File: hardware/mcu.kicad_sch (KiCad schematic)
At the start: 28 parts, among them J2 DS1021-1X3SF11-B, SW1 BOOT / PTS810, SW2 RESET / PTS810, U2 ESP32-C6-WROOM-1, U4 RV-3028-C7

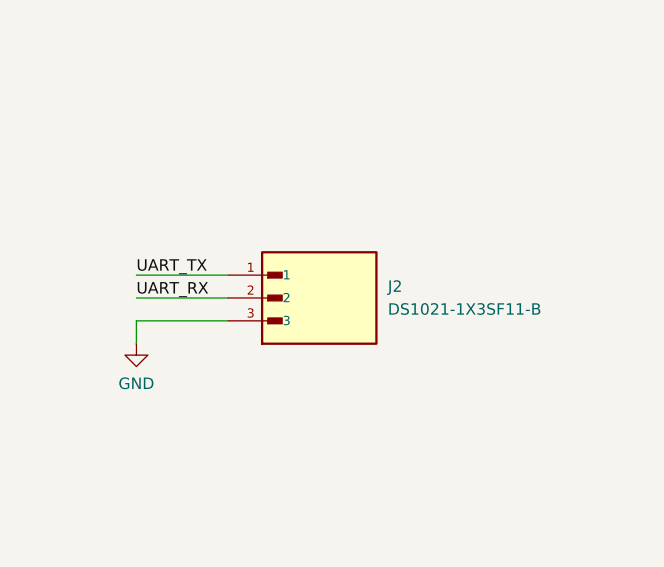
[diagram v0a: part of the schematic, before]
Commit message: J2 UART başlığını test noktalarıyla değiştir, ESP32 sembolünü yerelleştir
Kütüphane tabloları artık tamamen ${KIPRJMOD} göreli: harici mutlak yol
veya eksik kütüphane kalmadı, proje başka bir makinede olduğu gibi açılır.

J2 -> TP11/TP12/TP13
- J2 (DS1021-1X3SF11-B, 3 pinli UART başlığı) sembolü ve lib_symbols
  önbelleği mcu.kicad_sch'ten kaldırıldı.
- Yerine Connector:TestPoint ile TP11 (UART_TX), TP12 (UART_RX) ve
  TP13 (GND) eklendi; her biri J2'nin pinlerinin bulunduğu tellere bağlı.
- Sembol kütüphanesi başka bir makinenin Windows indirme klasörünü
  gösterdiği için sym-lib-table kaydı düştü; artık kullanılmayan
  CONNFLY_DS1021-1X3SF11-B footprint kütüphanesi de kaldırıldı.

ESP32-C6-WROOM-1 yerel kopya
- Sembol şematiğin lib_symbols önbelleğinden çıkarıldı, footprint
  espressif/kicad-libraries deposundan alındı; ikisi de
  hardware/libraries/PCM_Espressif.* altında.
- Takma ad şematiktekiyle aynı tutuldu, bu yüzden şematik düzenlemesi
  gerekmedi. Depoyu klonlayan birinin artık KiCad PCM eklentisini ayrıca
  kurması gerekmiyor.

Doğrulama
- Netlist karşılaştırması: 90 net sabit, yalnızca 3'ü değişti ve her biri
  birebir takas - J2.1->TP11.1, J2.2->TP12.1, J2.3->TP13.1.
- Sembolün 29 pini ile footprint'in 29 pad'i tam örtüşüyor.
- kicad-cli ERC: 7 -> 4 ihlal. Düşen üçü DS1021 ve iki PCM_Espressif
  uyarısı. Kalan 4 ihlal bu değişiklikten önce de vardı.

Co-Authored-By: Claude Opus 5 <noreply@anthropic.com>
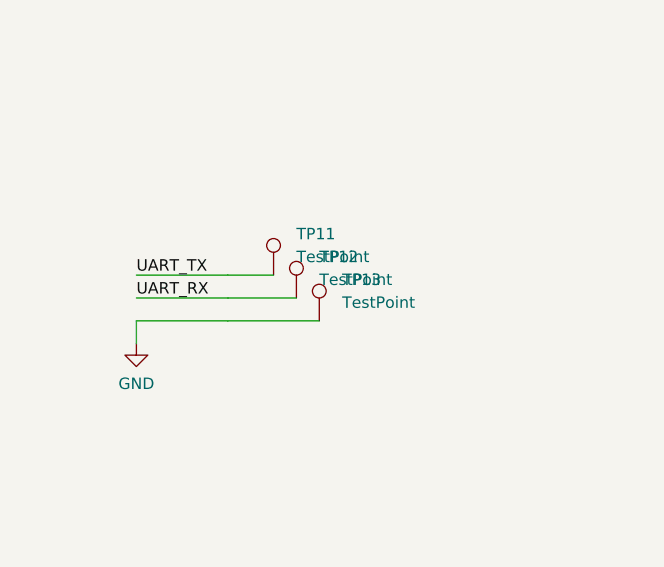
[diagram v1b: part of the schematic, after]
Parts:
- removed J2: DS1021-1X3SF11-B, CONNFLY_DS1021-1X3SF11-B:CONNFLY_DS1021-1X3SF11-B, symbol DS1021-1X3SF11-B:DS1021-1X3SF11-B
- added TP11, TP12, TP13: TestPoint, TestPoint:TestPoint_Pad_D1.0mm, symbol Connector:TestPoint
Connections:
- net GND: now also TP13.1
- net UART_RX: now also TP12.1
- net UART_TX: now also TP11.1
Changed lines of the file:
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@@
-	)
-	(symbol
-		(lib_id "DS1021-1X3SF11-B:DS1021-1X3SF11-B")
-		(at 247.65 146.05 0)
-		(unit 1)
-		(body_style 1)
-		(exclude_from_sim no)
-		(in_bom yes)
-		(on_board yes)
-		(in_pos_files yes)
-		(dnp no)
-		(fields_autoplaced yes)
-		(property "Reference" "J2"
-			(at 255.27 144.7799 0)
-			(show_name no)
-			(do_not_autoplace no)
-			(effects
-				(font
-					(size 1.27 1.27)
-				)
-				(justify left)
-			)
-		)
-		(property "Value" "DS1021-1X3SF11-B"
-			(at 255.27 147.3199 0)
-			(show_name no)
-			(do_not_autoplace no)
-			(effects
-				(font
-					(size 1.27 1.27)
-				)
-				(justify left)
-			)
-		)
-		(property "Footprint" "CONNFLY_DS1021-1X3SF11-B:CONNFLY_DS1021-1X3SF11-B"
-			(at 247.65 146.05 0)
-			(hide yes)
-			(show_name no)
-			(do_not_autoplace no)
-			(effects
-				(font
-					(size 1.27 1.27)
-				)
-				(justify bottom)
-			)
-		)
-		(property "Datasheet" ""
-			(at 247.65 146.05 0)
-			(hide yes)
-			(show_name no)
-			(do_not_autoplace no)
-			(effects
-				(font
-					(size 1.27 1.27)
-				)
-			)
-		)
-		(property "Description" "3 position 2.54mm single row vertical pin header through hole"
-			(at 247.65 146.05 0)
-			(hide yes)
-			(show_name no)
-			(do_not_autoplace no)
-			(effects
-				(font
-					(size 1.27 1.27)
-				)
-				(justify bottom)
-			)
-		)
-		(property "MF" "Connfly"
-			(at 247.65 146.05 0)
-			(hide yes)
-			(show_name no)
-			(do_not_autoplace no)
-			(effects
-				(font
-					(size 1.27 1.27)
-				)
-				(justify bottom)
-			)
-		)
-		(property "Package" "None"
-			(at 247.65 146.05 0)
-			(hide yes)
-			(show_name no)
-			(do_not_autoplace no)
-			(effects
-				(font
-					(size 1.27 1.27)
-				)
-				(justify bottom)
-			)
-		)
-		(property "Price" "None"
-			(at 247.65 146.05 0)
-			(hide yes)
-			(show_name no)
-			(do_not_autoplace no)
-			(effects
-				(font
-					(size 1.27 1.27)
-				)
-				(justify bottom)
-			)
-		)
-		(property "Check_prices" "https://www.snapeda.com/parts/DS1021-1X3SF11-B/Connfly/view-part/?ref=eda"
-			(at 247.65 146.05 0)
-			(hide yes)
-			(show_name no)
-			(do_not_autoplace no)
-			(effects
-				(font
-					(size 1.27 1.27)
-				)
-				(justify bottom)
-			)
-		)
-		(property "SnapEDA_Link" "https://www.snapeda.com/parts/DS1021-1X3SF11-B/Connfly/view-part/?ref=snap"
-			(at 247.65 146.05 0)
-			(hide yes)
-			(show_name no)
-			(do_not_autoplace no)
-			(effects
-				(font
-					(size 1.27 1.27)
-				)
-				(justify bottom)
-			)
-		)
-		(property "MP" "DS1021-1X3SF11-B"
-			(at 247.65 146.05 0)
-			(hide yes)
-			(show_name no)
-			(do_not_autoplace no)
-			(effects
-				(font
-					(size 1.27 1.27)
-				)
-				(justify bottom)
-			)
-		)
-		(property "Availability" "Not in stock"
-			(at 247.65 146.05 0)
-			(hide yes)
-			(show_name no)
-			(do_not_autoplace no)
-			(effects
-				(font
-					(size 1.27 1.27)
-				)
-				(justify bottom)
-			)
-		)
-		(property "MANUFACTURER" "CONNFLY"
-			(at 247.65 146.05 0)
-			(hide yes)
-			(show_name no)
-			(do_not_autoplace no)
-			(effects
-				(font
-					(size 1.27 1.27)
-				)
-				(justify bottom)
-			)
-		)
-		(property "MPN" "DS1021-1X3SF11-B"
-			(at 247.65 146.05 0)
-			(hide yes)
-			(show_name no)
-			(do_not_autoplace no)
-			(effects
-				(font
-					(size 1.27 1.27)
-				)
-			)
-		)
-		(pin "3"
-		)
-		(pin "1"
-		)
-		(pin "2"
-		)
-		(instances
-			(project "gopo"
-				(path "/a43081a6-9aa2-4898-9347-bbcb5849dafd/d73c21d5-7478-4a02-ac94-6607c580f283"
-					(reference "J2")
-					(unit 1)
-				)
-			)
-		)
 	)
 	(symbol
@@
 				)
 			)
+		)
+	)
+	(wire
+		(pts
+			(xy 237.49 143.51) (xy 242.57 143.51)
+		)
+		(stroke
+			(width 0)
+			(type default)
+		)
+	)
+	(wire
+		(pts
+			(xy 237.49 146.05) (xy 245.11 146.05)
+		)
+		(stroke
+			(width 0)
+			(type default)
+		)
+	)
+	(wire
+		(pts
+			(xy 237.49 148.59) (xy 247.65 148.59)
+		)
+		(stroke
+			(width 0)
+			(type default)
+		)
+	)
+	(symbol
+		(lib_id "Connector:TestPoint")
+		(at 242.57 143.51 0)
+		(unit 1)
+		(body_style 1)
+		(exclude_from_sim no)
+		(in_bom yes)
+		(on_board yes)
+		(in_pos_files yes)
+		(dnp no)
+		(fields_autoplaced yes)
+		(property "Reference" "TP11"
+			(at 245.11 138.9379 0)
+			(show_name no)
+			(do_not_autoplace no)
+			(effects
+				(font
+					(size 1.27 1.27)
+				)
+				(justify left)
+			)
+		)
+		(property "Value" "TestPoint"
+			(at 245.11 141.4779 0)
+			(show_name no)
+			(do_not_autoplace no)
+			(effects
+				(font
+					(size 1.27 1.27)
+				)
+				(justify left)
+			)
+		)
+		(property "Footprint" "TestPoint:TestPoint_Pad_D1.0mm"
+			(at 247.65 143.51 0)
+			(hide yes)
+			(show_name no)
+			(do_not_autoplace no)
+			(effects
+				(font
+					(size 1.27 1.27)
+				)
+			)
+		)
+		(property "Datasheet" "~"
+			(at 242.57 143.51 0)
+			(hide yes)
+			(show_name no)
+			(do_not_autoplace no)
+			(effects
+				(font
+					(size 1.27 1.27)
+				)
+			)
+		)
+		(property "Description" "test point"
+			(at 242.57 143.51 0)
+			(hide yes)
+			(show_name no)
+			(do_not_autoplace no)
+			(effects
+				(font
+					(size 1.27 1.27)
+				)
+			)
+		)
+		(pin "1"
+		)
+		(instances
+			(project "gopo"
+				(path "/a43081a6-9aa2-4898-9347-bbcb5849dafd/d73c21d5-7478-4a02-ac94-6607c580f283"
+					(reference "TP11")
+					(unit 1)
+				)
+			)
+		)
+	)
+	(symbol
+		(lib_id "Connector:TestPoint")
+		(at 245.11 146.05 0)
+		(unit 1)
+		(body_style 1)
+		(exclude_from_sim no)
+		(in_bom yes)
+		(on_board yes)
+		(in_pos_files yes)
+		(dnp no)
+		(fields_autoplaced yes)
+		(property "Reference" "TP12"
+			(at 247.65 141.4779 0)
+			(show_name no)
+			(do_not_autoplace no)
+			(effects
+				(font
+					(size 1.27 1.27)
+				)
+				(justify left)
+			)
+		)
+		(property "Value" "TestPoint"
+			(at 247.65 144.0179 0)
+			(show_name no)
+			(do_not_autoplace no)
+			(effects
+				(font
+					(size 1.27 1.27)
+				)
+				(justify left)
+			)
+		)
+		(property "Footprint" "TestPoint:TestPoint_Pad_D1.0mm"
+			(at 250.19 146.05 0)
+			(hide yes)
+			(show_name no)
+			(do_not_autoplace no)
+			(effects
+				(font
+					(size 1.27 1.27)
+				)
+			)
+		)
+		(property "Datasheet" "~"
+			(at 245.11 146.05 0)
+			(hide yes)
+			(show_name no)
+			(do_not_autoplace no)
+			(effects
+				(font
+					(size 1.27 1.27)
+				)
+			)
+		)
+		(property "Description" "test point"
+			(at 245.11 146.05 0)
+			(hide yes)
+			(show_name no)
+			(do_not_autoplace no)
+			(effects
+				(font
+					(size 1.27 1.27)
+				)
+			)
+		)
+		(pin "1"
+		)
+		(instances
+			(project "gopo"
+				(path "/a43081a6-9aa2-4898-9347-bbcb5849dafd/d73c21d5-7478-4a02-ac94-6607c580f283"
+					(reference "TP12")
+					(unit 1)
+				)
+			)
+		)
+	)
+	(symbol
+		(lib_id "Connector:TestPoint")
+		(at 247.65 148.59 0)
+		(unit 1)
+		(body_style 1)
+		(exclude_from_sim no)
+		(in_bom yes)
+		(on_board yes)
+		(in_pos_files yes)
+		(dnp no)
+		(fields_autoplaced yes)
+		(property "Reference" "TP13"
+			(at 250.19 144.0179 0)
+			(show_name no)
+			(do_not_autoplace no)
+			(effects
+				(font
+					(size 1.27 1.27)
+				)
+				(justify left)
+			)
+		)
+		(property "Value" "TestPoint"
+			(at 250.19 146.5579 0)
+			(show_name no)
+			(do_not_autoplace no)
+			(effects
+				(font
+					(size 1.27 1.27)
+				)
+				(justify left)
+			)
+		)
+		(property "Footprint" "TestPoint:TestPoint_Pad_D1.0mm"
+			(at 252.73 148.59 0)
+			(hide yes)
+			(show_name no)
+			(do_not_autoplace no)
+			(effects
+				(font
+					(size 1.27 1.27)
+				)
+			)
+		)
+		(property "Datasheet" "~"
+			(at 247.65 148.59 0)
+			(hide yes)
+			(show_name no)
+			(do_not_autoplace no)
+			(effects
+				(font
+					(size 1.27 1.27)
+				)
+			)
+		)
+		(property "Description" "test point"
+			(at 247.65 148.59 0)
+			(hide yes)
+			(show_name no)
+			(do_not_autoplace no)
+			(effects
+				(font
+					(size 1.27 1.27)
+				)
+			)
+		)
+		(pin "1"
+		)
+		(instances
+			(project "gopo"
+				(path "/a43081a6-9aa2-4898-9347-bbcb5849dafd/d73c21d5-7478-4a02-ac94-6607c580f283"
+					(reference "TP13")
+					(unit 1)
+				)
+			)

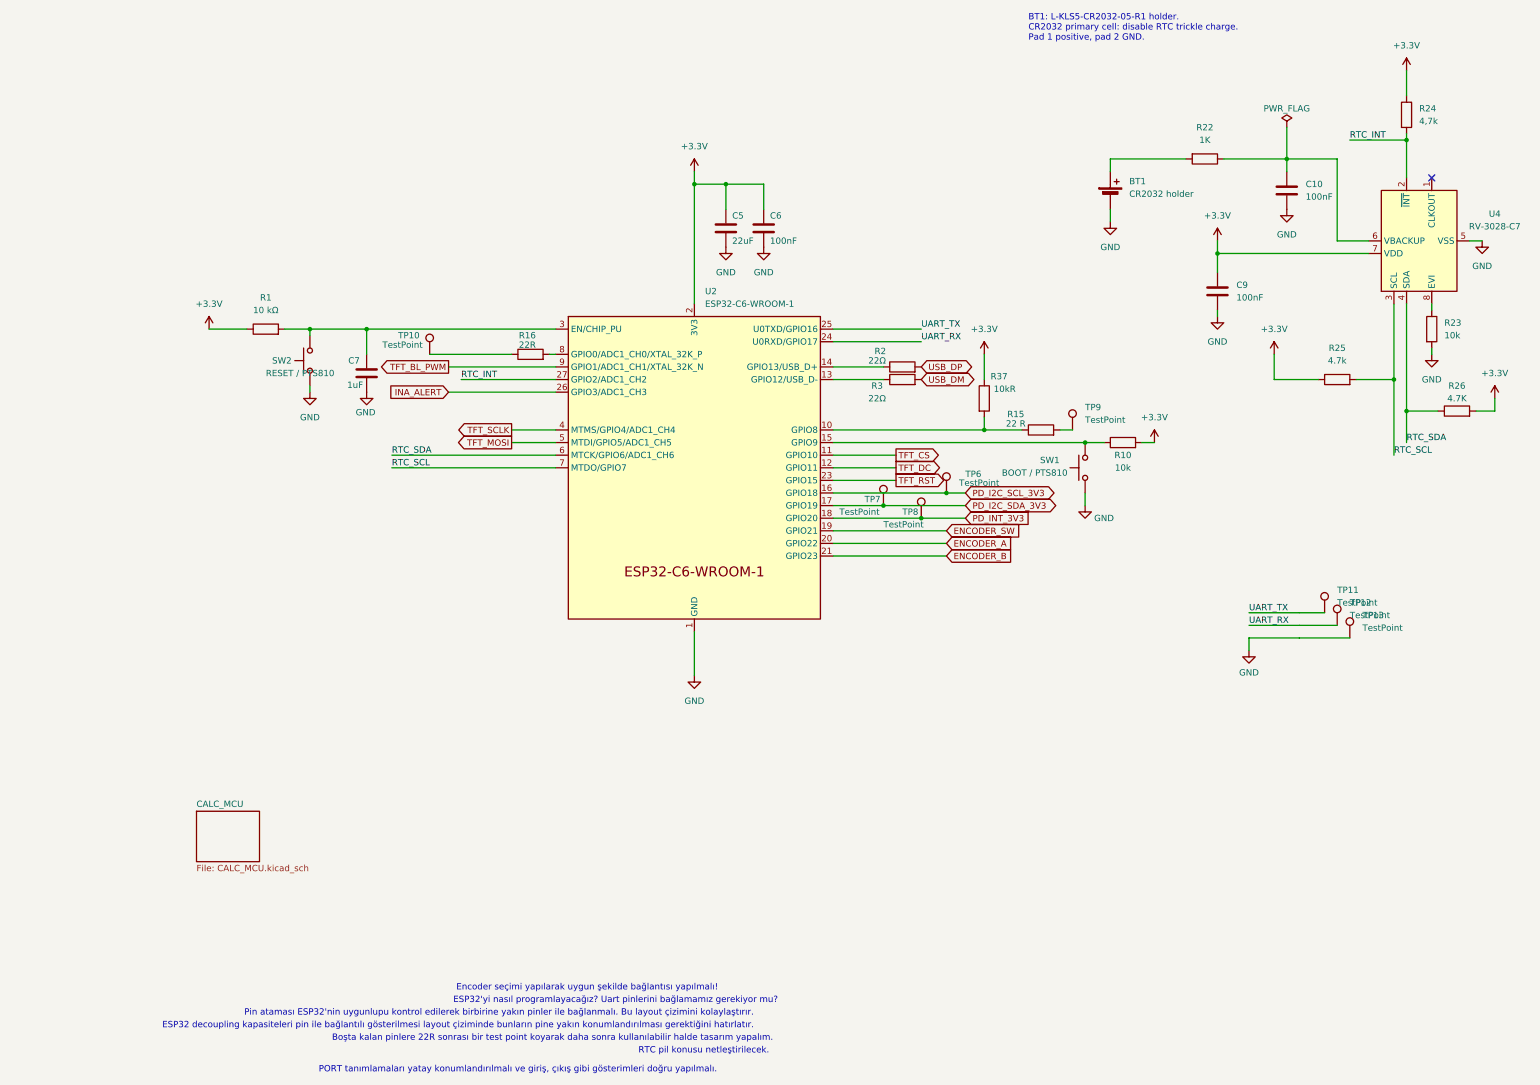
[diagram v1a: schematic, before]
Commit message: usb_pd_controller, mcu, powersensing: çizimleri yeniden düzenle, SDA dönüştürücüsünü bağla
Çizim (netlist aşağıdaki düzeltme dışında aynı)
- usb_pd_controller: üç blok (AP33772S kontrolcü, VBUS şönt + çıkış
  anahtarı, I2C seviye dönüştürücü). Q3/Q4 kapıları tek tel hattıyla,
  Q3 ang 90 + mirror y. TestPoint değer yazıları gizli.
- mcu: ESP32, RTC ve test noktası blokları. Sağ kenar satırları kesişmesiz;
  GPIO8 strap ağı satır sonunda, GPIO9 BOOT ağı dıştan aşağı. EN RC + RESET
  IC'nin üstüne alındı. UART/I2C/INT test noktaları etiketle ayrı blokta.
- powersensing: INA228 bloğu, şönt Kelvin bağlantısı kesişmesiz.

Devre düzeltmesi (kullanıcı onaylı)
- SDA seviye dönüştürücüsü kopuktu: R6.2 ve Q2.D bağlı değildi,
  PD_I2C_SDA_5V etiketi boştaydı. SCL tarafıyla (R5/Q1) simetrik bağlandı.
- Netlist farkı: PD_I2C_SDA_5V += Q2.3, R6.2;
  unconnected-(Q2-D-Pad3) ve unconnected-(R6-Pad2) kalktı.
- ERC 5 -> 2 (0 hata). Kalanlar: TL431DBZ lib_symbol_mismatch, OUT_EN
  isolated_pin_label (GPIO seçimi bekliyor).

Co-Authored-By: Claude Opus 5 <noreply@anthropic.com>
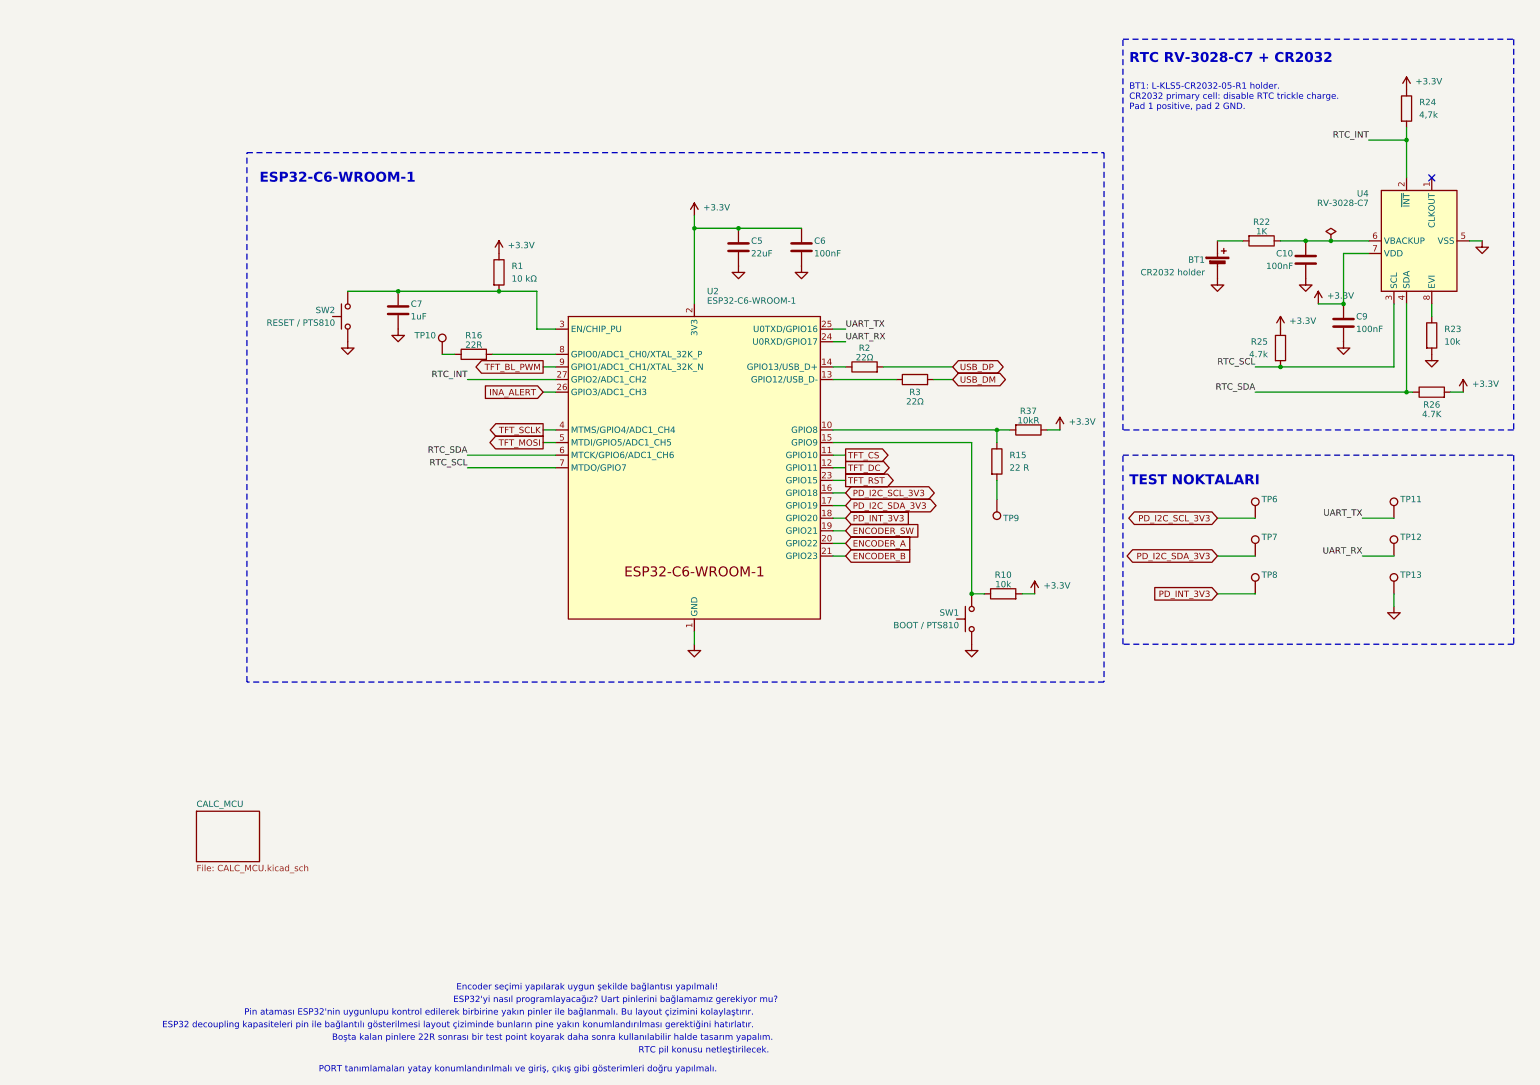
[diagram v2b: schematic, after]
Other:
- note added: "ESP32-C6-WROOM-1"
- note added: "RTC RV-3028-C7 + CR2032"
- note added: "TEST NOKTALARI"
- moved on the sheet: BT1, C10, C5, C6, C7, C9, R1, R10, R15, R16, R2, R22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
